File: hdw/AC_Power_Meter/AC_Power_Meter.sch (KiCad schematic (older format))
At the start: 0 parts

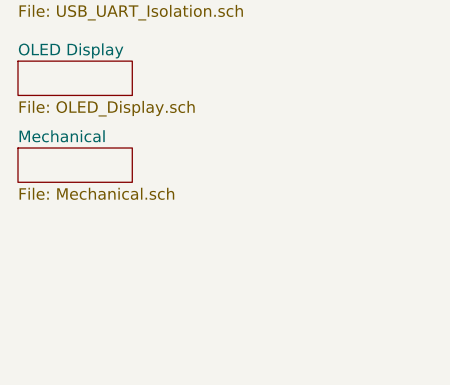
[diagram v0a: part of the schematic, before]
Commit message: Added zero cross detect circuit
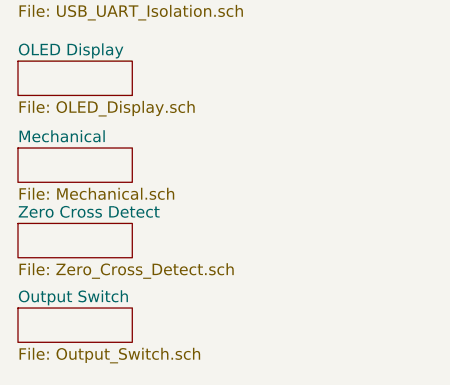
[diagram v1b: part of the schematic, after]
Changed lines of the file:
@@
 $Descr A 11000 8500
 encoding utf-8
-Sheet 1 13
+Sheet 1 15
 Title ""
 Date "2018-10-01"
@@
 F1 "Mechanical.sch" 50
 $EndSheet
+$Sheet
+S 2170 6360 500  150
+U 5BB31311
+F0 "Zero Cross Detect" 50
+F1 "Zero_Cross_Detect.sch" 50
+$EndSheet
+$Sheet
+S 2170 6730 500  150
+U 5BB31314
+F0 "Output Switch" 50
+F1 "Output_Switch.sch" 50
+$EndSheet
 $EndSCHEMATC

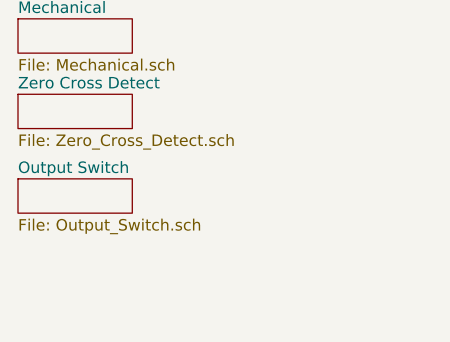
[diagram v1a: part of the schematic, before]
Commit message: Added +3.3V power supply, +12V window comparator, a few design files
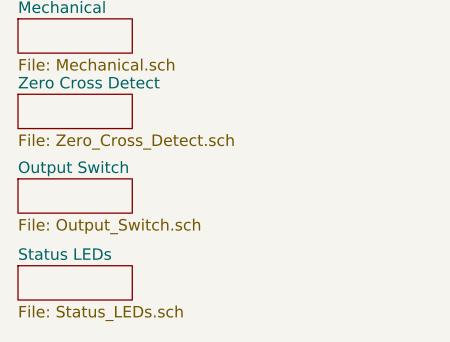
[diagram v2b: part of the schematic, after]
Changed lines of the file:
@@
 $Descr A 11000 8500
 encoding utf-8
-Sheet 1 15
+Sheet 1 16
 Title ""
 Date "2018-10-01"
@@
 F1 "Output_Switch.sch" 50
 $EndSheet
+$Sheet
+S 2170 7110 500  150
+U 5BB7FA89
+F0 "Status LEDs" 50
+F1 "Status_LEDs.sch" 50
+$EndSheet
 $EndSCHEMATC

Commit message: Added MU logo and titles to all sheets
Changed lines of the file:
@@
 $EndDescr
 $Sheet
-S 2170 1480 500  150
+S 2980 1420 500  150
 U 5BB27B1A
 F0 "AC Input" 50
@@
 $EndSheet
 $Sheet
-S 2170 1950 500  150
+S 2980 1890 500  150
 U 5BB27B24
 F0 "AC Current Sensor" 50
@@
 $EndSheet
 $Sheet
-S 2170 2390 500  150
+S 2980 2330 500  150
 U 5BB27B36
 F0 "AC Output" 50
@@
 $EndSheet
 $Sheet
-S 2170 2790 500  150
+S 2980 2730 500  150
 U 5BB27B51
 F0 "POS12 Power Supply" 50
@@
 $EndSheet
 $Sheet
-S 2170 3260 500  150
+S 2980 3200 500  150
 U 5BB27B73
 F0 "POS3P3 Power Supply" 50
@@
 $EndSheet
 $Sheet
-S 2170 3650 500  150
+S 2980 3590 500  150
 U 5BB27B84
 F0 "Microcontroller" 50
@@
 $EndSheet
 $Sheet
-S 2170 4030 500  150
+S 2980 3970 500  150
 U 5BB27BA3
 F0 "Microcontroller Programming" 50
@@
 $EndSheet
 $Sheet
-S 2170 4430 500  150
+S 2980 4370 500  150
 U 5BB27BB5
 F0 "Sensor Signal Conditioning" 50
@@
 $EndSheet
 $Sheet
-S 2170 4860 500  150
+S 2980 4800 500  150
 U 5BB27BCC
 F0 "USB UART Bridge" 50
@@
 $EndSheet
 $Sheet
-S 2170 5230 500  150
+S 2980 5170 500  150
 U 5BB27BE1
 F0 "USB UART Isolation" 50
@@
 $EndSheet
 $Sheet
-S 2170 5650 500  150
+S 2980 5590 500  150
 U 5BB27BF7
 F0 "OLED Display" 50
@@
 $EndSheet
 $Sheet
-S 2170 6030 500  150
+S 2980 5970 500  150
 U 5BB27C33
 F0 "Mechanical" 50
@@
 $EndSheet
 $Sheet
-S 2170 6360 500  150
+S 2980 6300 500  150
 U 5BB31311
 F0 "Zero Cross Detect" 50
@@
 $EndSheet
 $Sheet
-S 2170 6730 500  150
+S 2980 6670 500  150
 U 5BB31314
 F0 "Output Switch" 50
@@
 $EndSheet
 $Sheet
-S 2170 7110 500  150
+S 2980 7050 500  150
 U 5BB7FA89
 F0 "Status LEDs" 50
 F1 "Status_LEDs.sch" 50
 $EndSheet
+$Comp
+L Mu_Logo:LOGO #G?
+U 1 1 5BBF0B97
+P 9900 1000
+F 0 "#G?" H 9900 670 60  0001 C CNN
+F 1 "LOGO" H 9900 1330 60  0001 C CNN
+F 2 "" H 9900 1000 50  0001 C CNN
+F 3 "" H 9900 1000 50  0001 C CNN
+	1    9900 1000
+	1    0    0    -1
+$EndComp
 $EndSCHEMATC

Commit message: Updated MU logo to crisper image
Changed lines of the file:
@@
 $EndSheet
 $Comp
-L Mu_Logo:LOGO #G?
-U 1 1 5BBF0B97
-P 9900 1000
-F 0 "#G?" H 9900 670 60  0001 C CNN
-F 1 "LOGO" H 9900 1330 60  0001 C CNN
-F 2 "" H 9900 1000 50  0001 C CNN
-F 3 "" H 9900 1000 50  0001 C CNN
-	1    9900 1000
+L Custom_Library:MU_Logo #G?
+U 1 1 5BB67CD7
+P 9900 1100
+F 0 "#G?" H 9900 614 60  0001 C CNN
+F 1 "MU_Logo" H 9900 1586 60  0001 C CNN
+F 2 "" H 9900 1100 50  0001 C CNN
+F 3 "" H 9900 1100 50  0001 C CNN
+	1    9900 1100
 	1    0    0    -1
 $EndComp

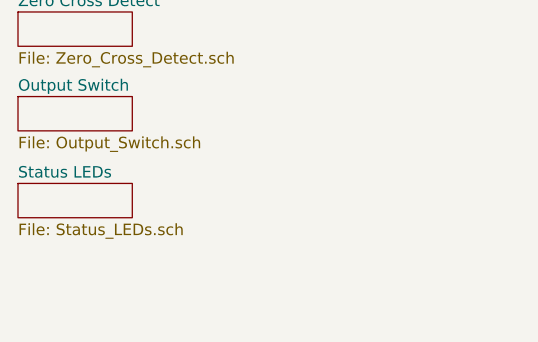
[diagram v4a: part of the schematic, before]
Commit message: Added pushbuttons sheet, prelim wiring on micro
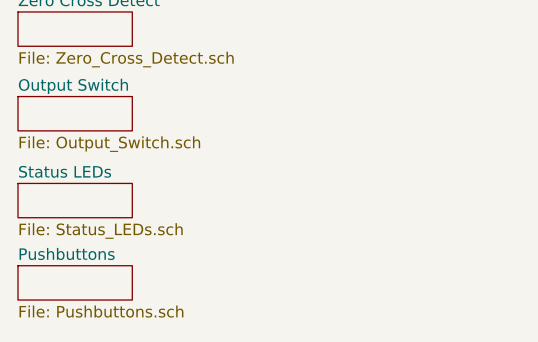
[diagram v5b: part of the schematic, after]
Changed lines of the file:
@@
 $Descr A 11000 8500
 encoding utf-8
-Sheet 1 16
+Sheet 1 17
 Title ""
 Date "2018-10-01"
@@
 	1    0    0    -1
 $EndComp
+$Sheet
+S 2980 7410 500  150
+U 5BC25FFE
+F0 "Pushbuttons" 50
+F1 "Pushbuttons.sch" 50
+$EndSheet
 $EndSCHEMATC

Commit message: Rewired a few micro symbols, add FMW notes
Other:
- note added: "1. AC Input\n\n\n2. AC Current Sensor\n\n\n3. AC Output\n\n\n4. +12V Power Supply\n\n\n5. +3.3V Power Supply\n\n\n6. Microcontroller\n\n\n7. Microcontoller Programming\n\n\n8. Sensor Signal Conditioning\n\n\n9. USB UART Bridge\n\n\n10. USB UART Isolation\n\n\n11. OLED Display"
- note added: "12. Mechanical\n\n\n13. Zero Cross Detect\n\n\n14. Output Switch\n\n\n15. Status LEDs\n\n\n16. Pushbuttons\n\n\n17. Firmware Notes"
- note added: "AC Energy Meter/Dimmer"
- note added: "Table of Contents:"
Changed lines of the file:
@@
 $Descr A 11000 8500
 encoding utf-8
-Sheet 1 17
+Sheet 1 18
 Title ""
 Date "2018-10-01"
@@
 $EndDescr
 $Sheet
-S 2980 1420 500  150
+S 3470 1440 500  150
 U 5BB27B1A
 F0 "AC Input" 50
@@
 $EndSheet
 $Sheet
-S 2980 1890 500  150
+S 3470 1910 500  150
 U 5BB27B24
 F0 "AC Current Sensor" 50
@@
 $EndSheet
 $Sheet
-S 2980 2330 500  150
+S 3470 2380 500  150
 U 5BB27B36
 F0 "AC Output" 50
@@
 $EndSheet
 $Sheet
-S 2980 2730 500  150
+S 3470 2850 500  150
 U 5BB27B51
 F0 "POS12 Power Supply" 50
@@
 $EndSheet
 $Sheet
-S 2980 3200 500  150
+S 3470 3320 500  150
 U 5BB27B73
 F0 "POS3P3 Power Supply" 50
@@
 $EndSheet
 $Sheet
-S 2980 3590 500  150
+S 3470 3790 500  150
 U 5BB27B84
 F0 "Microcontroller" 50
@@
 $EndSheet
 $Sheet
-S 2980 3970 500  150
+S 3470 4260 500  150
 U 5BB27BA3
 F0 "Microcontroller Programming" 50
@@
 $EndSheet
 $Sheet
-S 2980 4370 500  150
+S 3470 4730 500  150
 U 5BB27BB5
 F0 "Sensor Signal Conditioning" 50
@@
 $EndSheet
 $Sheet
-S 2980 4800 500  150
+S 3470 5200 500  150
 U 5BB27BCC
 F0 "USB UART Bridge" 50
@@
 $EndSheet
 $Sheet
-S 2980 5170 500  150
+S 3470 5670 500  150
 U 5BB27BE1
 F0 "USB UART Isolation" 50
@@
 $EndSheet
 $Sheet
-S 2980 5590 500  150
+S 3470 6140 500  150
 U 5BB27BF7
 F0 "OLED Display" 50
@@
 $EndSheet
 $Sheet
-S 2980 5970 500  150
+S 7720 1440 500  150
 U 5BB27C33
 F0 "Mechanical" 50
@@
 $EndSheet
 $Sheet
-S 2980 6300 500  150
+S 7720 1910 500  150
 U 5BB31311
 F0 "Zero Cross Detect" 50
@@
 $EndSheet
 $Sheet
-S 2980 6670 500  150
+S 7720 2380 500  150
 U 5BB31314
 F0 "Output Switch" 50
@@
 $EndSheet
 $Sheet
-S 2980 7050 500  150
+S 7720 2850 500  150
 U 5BB7FA89
 F0 "Status LEDs" 50
@@
 $EndSheet
 $Comp
-L Custom_Library:MU_Logo #G?
+L Custom_Library:MU_Logo #G101
 U 1 1 5BB67CD7
 P 9900 1100
-F 0 "#G?" H 9900 614 60  0001 C CNN
+F 0 "#G101" H 9900 614 60  0001 C CNN
 F 1 "MU_Logo" H 9900 1586 60  0001 C CNN
 F 2 "" H 9900 1100 50  0001 C CNN
@@
 $EndComp
 $Sheet
-S 2980 7410 500  150
+S 7720 3320 500  150
 U 5BC25FFE
 F0 "Pushbuttons" 50
 F1 "Pushbuttons.sch" 50
 $EndSheet
+Text Notes 540  690  0    100  ~ 20
+Table of Contents:
+Text Notes 4070 780  0    150  ~ 30
+AC Energy Meter/Dimmer
+Text Notes 770  6260 0    100  ~ 0
+1. AC Input\n\n\n2. AC Current Sensor\n\n\n3. AC Output\n\n\n4. +12V Power Supply\n\n\n5. +3.3V Power Supply\n\n\n6. Microcontroller\n\n\n7. Microcontoller Programming\n\n\n8. Sensor Signal Conditioning\n\n\n9. USB UART Bridge\n\n\n10. USB UART Isolation\n\n\n11. OLED Display
+Text Notes 5650 3940 0    100  ~ 0
+12. Mechanical\n\n\n13. Zero Cross Detect\n\n\n14. Output Switch\n\n\n15. Status LEDs\n\n\n16. Pushbuttons\n\n\n17. Firmware Notes
+$Sheet
+S 7720 3790 500  150
+U 5BB83979
+F0 "Firmware Notes" 50
+F1 "Firmware_Notes.sch" 50
+$EndSheet
 $EndSCHEMATC

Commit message: Updated most footprints
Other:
- note added: "AC Power Meter/Dimmer"
- note removed: "AC Energy Meter/Dimmer"
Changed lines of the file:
@@
 Table of Contents:
 Text Notes 4070 780  0    150  ~ 30
-AC Energy Meter/Dimmer
+AC Power Meter/Dimmer
 Text Notes 770  6260 0    100  ~ 0
 1. AC Input\n\n\n2. AC Current Sensor\n\n\n3. AC Output\n\n\n4. +12V Power Supply\n\n\n5. +3.3V Power Supply\n\n\n6. Microcontroller\n\n\n7. Microcontoller Programming\n\n\n8. Sensor Signal Conditioning\n\n\n9. USB UART Bridge\n\n\n10. USB UART Isolation\n\n\n11. OLED Display

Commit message: Serious BOM scrubbing to drive price down
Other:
- note added: "12. Mechanical\n\n\n13. Zero Cross Detect\n\n\n14. Output Switch\n\n\n15. Status LEDs\n\n\n17. Firmware Notes"
- note added: "AC Power Meter"
- note removed: "12. Mechanical\n\n\n13. Zero Cross Detect\n\n\n14. Output Switch\n\n\n15. Status LEDs\n\n\n16. Pushbuttons\n\n\n17. Firmware Notes"
- note removed: "AC Power Meter/Dimmer"
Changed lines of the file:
@@
 $Descr A 11000 8500
 encoding utf-8
-Sheet 1 18
+Sheet 1 17
 Title ""
 Date "2018-10-01"
@@
 $EndSheet
 $Sheet
-S 7720 1910 500  150
-U 5BB31311
-F0 "Zero Cross Detect" 50
-F1 "Zero_Cross_Detect.sch" 50
-$EndSheet
-$Sheet
-S 7720 2380 500  150
-U 5BB31314
-F0 "Output Switch" 50
-F1 "Output_Switch.sch" 50
-$EndSheet
-$Sheet
 S 7720 2850 500  150
 U 5BB7FA89
@@
 	1    0    0    -1
 $EndComp
-$Sheet
-S 7720 3320 500  150
-U 5BC25FFE
-F0 "Pushbuttons" 50
-F1 "Pushbuttons.sch" 50
-$EndSheet
 Text Notes 540  690  0    100  ~ 20
 Table of Contents:
 Text Notes 4070 780  0    150  ~ 30
-AC Power Meter/Dimmer
+AC Power Meter
 Text Notes 770  6260 0    100  ~ 0
 1. AC Input\n\n\n2. AC Current Sensor\n\n\n3. AC Output\n\n\n4. +12V Power Supply\n\n\n5. +3.3V Power Supply\n\n\n6. Microcontroller\n\n\n7. Microcontoller Programming\n\n\n8. Sensor Signal Conditioning\n\n\n9. USB UART Bridge\n\n\n10. USB UART Isolation\n\n\n11. OLED Display
-Text Notes 5650 3940 0    100  ~ 0
-12. Mechanical\n\n\n13. Zero Cross Detect\n\n\n14. Output Switch\n\n\n15. Status LEDs\n\n\n16. Pushbuttons\n\n\n17. Firmware Notes
+Text Notes 5660 3480 0    100  ~ 0
+12. Mechanical\n\n\n13. Zero Cross Detect\n\n\n14. Output Switch\n\n\n15. Status LEDs\n\n\n17. Firmware Notes
 $Sheet
-S 7720 3790 500  150
+S 7720 3350 500  150
 U 5BB83979
 F0 "Firmware Notes" 50
 F1 "Firmware_Notes.sch" 50
 $EndSheet
+$Sheet
+S 7720 1940 500  150
+U 5BBE5EA4
+F0 "Zero Cross Detect" 50
+F1 "Zero_Cross_Detect.sch" 50
+$EndSheet
+$Sheet
+S 7720 2440 500  150
+U 5BBE5EA9
+F0 "Output Switch" 50
+F1 "Output_Switch.sch" 50
+$EndSheet
 $EndSCHEMATC
